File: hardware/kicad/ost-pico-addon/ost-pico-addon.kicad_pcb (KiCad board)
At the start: 2 copper layers, 70 x 60 mm, 13 parts, among them J1 Conn_01x09_Male, J2 104031-0811, J3 Conn_01x08_Male, J4 Conn_01x03_Male, U1 Pico

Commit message: pinout and routing changes
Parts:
- removed REF** (x6): MountingHole_2.2mm_M2_ISO7380_Pad, MountingHole:MountingHole_2.2mm_M2_ISO7380_Pad
- J3: value Conn_01x08_Male -> buttons; footprint Connector_PinHeader_2.54mm:PinHeader_1x08_P2.54mm_Vertical -> Connector_PinSocket_2.54mm:PinSocket_2x08_P2.54mm_Vertical
- moved J3 17.8 mm to (105.4, 129.5), turned to 0 degrees
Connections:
- J3 pad 1: +3.3V -> BUTTON_4
- J3 pad 3: ROT_1 -> BUTTON_3
- J3 pad 4: ROT_2 -> GND
- J3 pad 5: BUTTON_1 -> BUTTON_2
- J3 pad 6: BUTTON_2 -> GND
- J3 pad 7: BUTTON_3 -> BUTTON_1
- J3 pad 8: BUTTON_4 -> GND
- U1 pad 11: unconnected-(U1-Pad11) -> BUTTON_4
- U1 pad 12: unconnected-(U1-Pad12) -> BUTTON_3
- U1 pad 14: unconnected-(U1-Pad14) -> BUTTON_2
- U1 pad 15: unconnected-(U1-Pad15) -> BUTTON_1
- U1 pad 16: unconnected-(U1-Pad16) -> ROT_2
- U1 pad 17: unconnected-(U1-Pad17) -> ROT_1
- U1 pad 21: BUTTON_2 -> unconnected-(U1-GPIO16-Pad21)
- U1 pad 22: BUTTON_1 -> unconnected-(U1-GPIO17-Pad22)
- U1 pad 24: ROT_2 -> unconnected-(U1-GPIO18-Pad24)
- U1 pad 25: ROT_1 -> unconnected-(U1-GPIO19-Pad25)
- U1 pad 4: BUTTON_3 -> unconnected-(U1-GPIO2-Pad4)
- U1 pad 5: BUTTON_4 -> unconnected-(U1-GPIO3-Pad5)
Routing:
- net GND: track 223.4 -> 8.33 mm, vias 0 -> 2
- net SD_DET: track 139.9 -> 71.9 mm
- net BUTTON_2: track 82.8 -> 37.3 mm
- net BUTTON_1: track 79.0 -> 37.3 mm
- net ROT_1: track 78.4 -> 37.3 mm
- net ROT_2: track 68.4 -> 37.3 mm
- net BUTTON_4: track 57.7 -> 36.4 mm
- net BUTTON_3: track 50.7 -> 36.3 mm
- net +3.3V: track 133.4 -> 121.8 mm
- net SD_SPI_RX: track 36.6 -> 29.5 mm
- net SD_CS: track 33.6 -> 29.4 mm
- net SD_SPI_CLK: track 30.8 -> 29.3 mm
- added copper zone on B.Cu, net GND
- added copper zone on F.Cu, net GND

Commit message: change button port pinout
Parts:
- J3: footprint Connector_PinSocket_2.54mm:PinSocket_2x08_P2.54mm_Vertical -> Connector_PinHeader_2.54mm:PinHeader_2x07_P2.54mm_Vertical; moved to B.Cu
- turned J3 to 180 degrees
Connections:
- J3 pad 1: BUTTON_4 -> +3.3V
- J3 pad 11: ROT_1 -> ROT_2
- J3 pad 13: GND -> ROT_1
- J3 pad 14: GND -> ROT_BUTTON
- J3 pad 3: BUTTON_3 -> BUTTON_4
- J3 pad 5: BUTTON_2 -> BUTTON_3
- J3 pad 7: BUTTON_1 -> BUTTON_2
- J3 pad 9: ROT_2 -> BUTTON_1
- U1 pad 19: DBG_LED -> ROT_BUTTON
- U1 pad 20: SD_DET -> DBG_LED
- U1 pad 4: unconnected-(U1-GPIO2-Pad4) -> SD_DET
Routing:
- net ROT_BUTTON: track 0.00 -> 40.9 mm
- net SD_DET: track 71.9 -> 35.8 mm
- net +3.3V: track 121.8 -> 104.0 mm
- net GND: track 8.33 -> 3.28 mm, vias 2 -> 1
- net ROT_2: track 37.3 -> 36.3 mm
- net ROT_1: track 37.3 -> 36.3 mm
- net BUTTON_2: track 37.3 -> 36.3 mm
- net BUTTON_1: track 37.3 -> 36.3 mm
- net DBG_LED: track 12.9 -> 12.3 mm
- net BUTTON_4: track 36.4 -> 35.9 mm
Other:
- board text added: "3.3V BTN_4 BTN_3 BTN_2 BTN_1 ROT_2 ROT_1"
- board text added: "GND"
- board text added: "ROT_push"
- board text removed: "BTN_4 BTN_3 BTN_2 BTN_1 ROT_2 ROT_1 Gnd 3.3V"

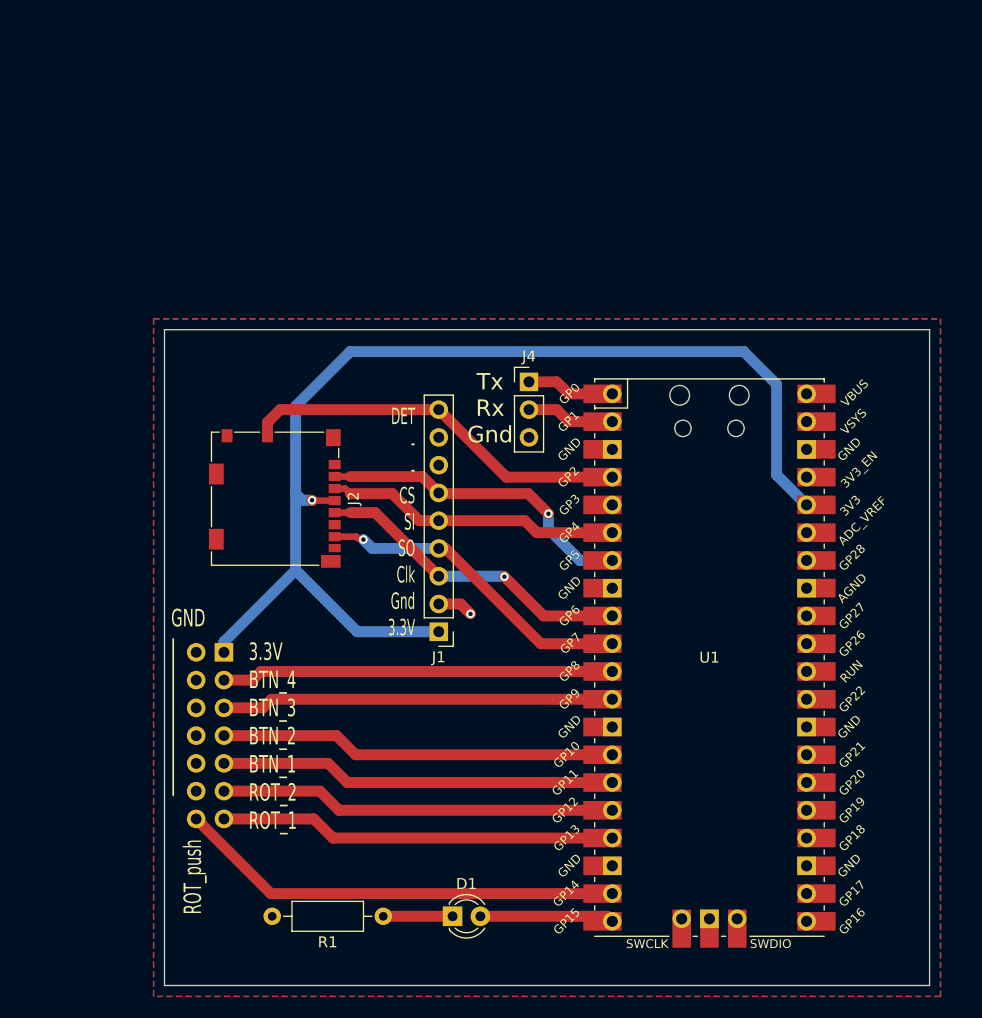
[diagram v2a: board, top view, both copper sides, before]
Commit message: editor v2 + usb host tests
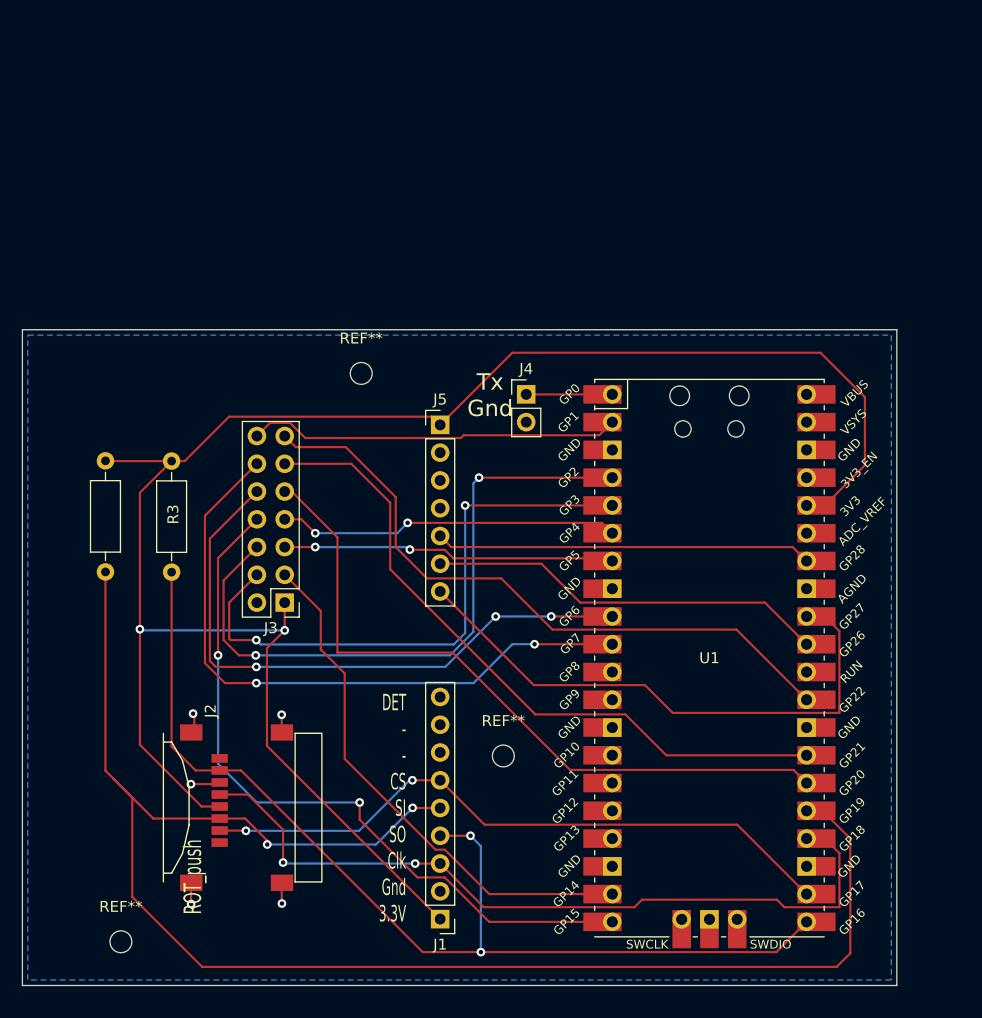
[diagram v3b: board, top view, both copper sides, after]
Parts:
- removed D1: LED, LED_THT:LED_D3.0mm
- removed R1: R_US, Resistor_THT:R_Axial_DIN0207_L6.3mm_D2.5mm_P10.16mm_Horizontal
- added J5: Conn_01x07_Pin, Connector_PinHeader_2.54mm:PinHeader_1x07_P2.54mm_Vertical, F.Cu at (125.2, 108.7)
- added R2: R_US, Resistor_THT:R_Axial_DIN0207_L6.3mm_D2.5mm_P10.16mm_Horizontal, F.Cu at (94.6, 112.0)
- added R3: R_US, Resistor_THT:R_Axial_DIN0207_L6.3mm_D2.5mm_P10.16mm_Horizontal, F.Cu at (100.7, 112.0)
- added REF**: MountingHole_2mm, MountingHole:MountingHole_2mm, F.Cu at (131.0, 139.0)
- added REF**: MountingHole_2mm, MountingHole:MountingHole_2mm, F.Cu at (96.0, 156.0)
- added REF**: MountingHole_2mm, MountingHole:MountingHole_2mm, F.Cu at (118.0, 104.0)
- J2: value 104031-0811 -> 47219-2001; footprint Connector_Card:microSD_HC_Molex_104031-0811 -> sdcard-libs:MOLEX_47219-2001
- J3: moved to F.Cu
- J4: value Conn_01x03_Male -> Conn_01x02_Pin; footprint Connector_PinHeader_2.54mm:PinHeader_1x03_P2.54mm_Vertical -> Connector_PinHeader_2.54mm:PinHeader_1x02_P2.54mm_Vertical
- moved J2 28.4 mm to (107.2, 143.7)
- moved J1 26.3 mm to (125.2, 153.9)
- moved J3 7.18 mm to (111.0, 125.0)
- moved J4 1.17 mm to (133.1, 105.9)
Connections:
- J1 pad 4: SD_SPI_RX -> SD_SPI_MISO
- J1 pad 5: SD_SPI_TX -> SD_SPI_MOSI
- J1 pad 9: SD_DET -> unconnected-(J1-Pin_9-Pad9)
- J2 pad 3: SD_SPI_TX -> SD_SPI_MOSI
- J2 pad 7: SD_SPI_RX -> SD_SPI_MISO
- J3 pad 10: GND -> ROT_1
- J3 pad 11: ROT_2 -> IO_2
- J3 pad 12: GND -> ROT_2
- J3 pad 13: ROT_1 -> IO_1
- J3 pad 3: BUTTON_4 -> IO_6
- J3 pad 4: GND -> KEY3
- J3 pad 5: BUTTON_3 -> IO_5
- J3 pad 6: GND -> KEY2
- J3 pad 7: BUTTON_2 -> IO_4
- J3 pad 8: GND -> KEY0
- J3 pad 9: BUTTON_1 -> IO_3
- J4 pad 2: DBG_RX -> GND
- U1 pad 10: SD_SPI_RX -> ROT_2
- U1 pad 11: BUTTON_4 -> unconnected-(U1-GPIO8-Pad11)
- U1 pad 12: BUTTON_3 -> unconnected-(U1-GPIO9-Pad12)
- U1 pad 14: BUTTON_2 -> unconnected-(U1-GPIO10-Pad14)
- U1 pad 15: BUTTON_1 -> unconnected-(U1-GPIO11-Pad15)
- U1 pad 16: ROT_2 -> unconnected-(U1-GPIO12-Pad16)
- U1 pad 17: ROT_1 -> unconnected-(U1-GPIO13-Pad17)
- U1 pad 19: ROT_BUTTON -> IO_6
- U1 pad 2: DBG_RX -> ROT_BUTTON
- U1 pad 20: DBG_LED -> KEY0
- U1 pad 21: unconnected-(U1-GPIO16-Pad21) -> SD_SPI_MISO
- U1 pad 22: unconnected-(U1-GPIO17-Pad22) -> SD_CS
- U1 pad 24: unconnected-(U1-GPIO18-Pad24) -> SD_SPI_CLK
- U1 pad 25: unconnected-(U1-GPIO19-Pad25) -> SD_SPI_MOSI
- U1 pad 26: unconnected-(U1-GPIO20-Pad26) -> IO_3
- U1 pad 27: unconnected-(U1-GPIO21-Pad27) -> IO_2
- U1 pad 29: unconnected-(U1-GPIO22-Pad29) -> IO_1
- U1 pad 31: unconnected-(U1-GPIO26_ADC0-Pad31) -> I2S_SCLK
- U1 pad 32: unconnected-(U1-GPIO27_ADC1-Pad32) -> I2S_LRCK
- U1 pad 34: unconnected-(U1-GPIO28_ADC2-Pad34) -> I2S_DATA
- U1 pad 4: SD_DET -> KEY2
- U1 pad 5: unconnected-(U1-GPIO3-Pad5) -> KEY3
- U1 pad 6: SD_SPI_TX -> IO_4
- U1 pad 7: SD_CS -> IO_5
- U1 pad 9: SD_SPI_CLK -> ROT_1
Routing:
- net SD_SPI_MOSI: track 0.00 -> 149.2 mm, vias 0 -> 2
- net SD_SPI_MISO: track 0.00 -> 96.8 mm, vias 0 -> 2
- net +3.3V: track 104.0 -> 175.3 mm, vias 1 -> 2
- net KEY0: track 0.00 -> 66.8 mm, vias 0 -> 2
- net IO_3: track 0.00 -> 65.0 mm
- net IO_2: track 0.00 -> 62.4 mm
- net KEY2: track 0.00 -> 60.6 mm, vias 0 -> 2
- net IO_1: track 0.00 -> 60.4 mm
- net KEY3: track 0.00 -> 54.3 mm, vias 0 -> 2
- net I2S_LRCK: track 0.00 -> 52.2 mm
- net IO_6: track 0.00 -> 48.7 mm
- net SD_SPI_CLK: track 29.3 -> 71.8 mm, vias 1 -> 2
- net I2S_SCLK: track 0.00 -> 36.6 mm
- net BUTTON_2: track 36.3 -> 0.00 mm
- net BUTTON_1: track 36.3 -> 0.00 mm
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- removed copper zone on F.Cu, net GND
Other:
- board size 70 x 60 mm -> 80 x 60 mm
- board text added: "Tx Gnd"
- board text removed: "3.3V BTN_4 BTN_3 BTN_2 BTN_1 ROT_2 ROT_1"
- board text removed: "GND"
- board text removed: "Tx Rx Gnd"

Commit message: Pico audio with 3 audio chips (complex)
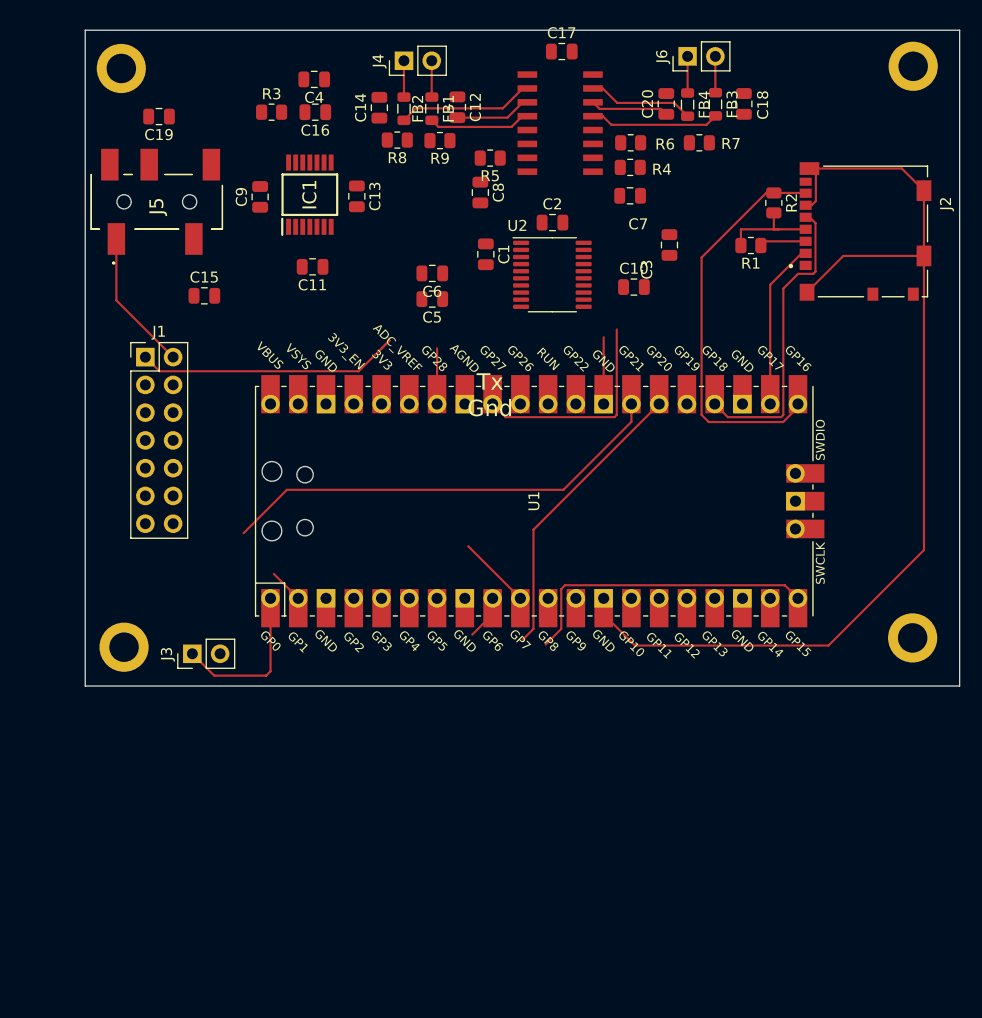
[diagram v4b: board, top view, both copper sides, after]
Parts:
- removed REF** (x3): MountingHole_2mm, MountingHole:MountingHole_2mm
- added C1: 2.2uF, Capacitor_SMD:C_0805_2012Metric, F.Cu at (129.4, 93.1)
- added C10: 1uF, Capacitor_SMD:C_0805_2012Metric, F.Cu at (142.9, 96.1)
- added C11: 1uF, Capacitor_SMD:C_0805_2012Metric, F.Cu at (113.5, 94.2)
- added C12: 270pF, Capacitor_SMD:C_0805_2012Metric, F.Cu at (126.8, 79.7)
- added C13: 47uF/6.3V/20%/X5R/C0805, Capacitor_SMD:C_0805_2012Metric, F.Cu at (117.6, 87.8)
- added C14: 270pF, Capacitor_SMD:C_0805_2012Metric, F.Cu at (119.7, 79.7)
- added C15: 47uF, Capacitor_SMD:C_0805_2012Metric, F.Cu at (103.7, 96.9)
- added C16: 47uF/6.3V/20%/X5R/C0805, Capacitor_SMD:C_0805_2012Metric, F.Cu at (113.8, 80.1)
- added C17: 100nF/50V/20%/Y5V/C0603, Capacitor_SMD:C_0805_2012Metric, F.Cu at (136.3, 74.5)
- added C18: 270pF, Capacitor_SMD:C_0805_2012Metric, F.Cu at (153.0, 79.3)
- added C19: 47uF, Capacitor_SMD:C_0805_2012Metric, F.Cu at (99.5, 80.5)
- added C2: 2.2uF, Capacitor_SMD:C_0805_2012Metric, F.Cu at (135.5, 90.2)
- added C20: 270pF, Capacitor_SMD:C_0805_2012Metric, F.Cu at (145.9, 79.3)
- added C3: 100nF, Capacitor_SMD:C_0805_2012Metric, F.Cu at (146.2, 92.2)
- added C4: 1uF, Capacitor_SMD:C_0805_2012Metric, F.Cu at (113.7, 77.1)
- added C5: 2.2uF, Capacitor_SMD:C_0805_2012Metric, F.Cu at (124.5, 97.2)
- added C6: 2.2uF, Capacitor_SMD:C_0805_2012Metric, F.Cu at (124.5, 94.8)
- added C7: 1uF, Capacitor_SMD:C_0805_2012Metric, F.Cu at (142.6, 87.8)
- added C8: 1uF, Capacitor_SMD:C_0805_2012Metric, F.Cu at (128.9, 87.5)
- added C9: 1uF, Capacitor_SMD:C_0805_2012Metric, F.Cu at (108.8, 87.8)
- added FB1: FB0805, Inductor_SMD:L_0805_2012Metric, F.Cu at (124.5, 79.8)
- added FB2: FB0805, Inductor_SMD:L_0805_2012Metric, F.Cu at (121.9, 79.8)
- added FB3: FB0805, Inductor_SMD:L_0805_2012Metric, F.Cu at (150.4, 79.4)
- added FB4: FB0805, Inductor_SMD:L_0805_2012Metric, F.Cu at (147.9, 79.4)
- added H1: MountingHole, MountingHole:MountingHole_2.7mm_M2.5_ISO14580_Pad, F.Cu at (96.0, 76.1)
- added H2: MountingHole, MountingHole:MountingHole_2.7mm_M2.5_ISO14580_Pad, F.Cu at (168.5, 75.9)
- added H3: MountingHole, MountingHole:MountingHole_2.7mm_M2.5_ISO14580_Pad, F.Cu at (168.4, 128.2)
- added H4: MountingHole, MountingHole:MountingHole_2.7mm_M2.5_ISO14580_Pad, F.Cu at (96.3, 129.1)
- added IC1: TPA6139A2PWR, audio:SOP65P640X120-14N, F.Cu at (113.3, 87.7)
- added J6: SPK_RIGHT, Connector_PinHeader_2.54mm:PinHeader_1x02_P2.54mm_Vertical, F.Cu at (147.9, 75.0)
- added R1: 10K, Resistor_SMD:R_0805_2012Metric, F.Cu at (153.7, 92.3)
- added R4: 10k, Resistor_SMD:R_0805_2012Metric, F.Cu at (142.6, 85.2)
- added R5: 10k, Resistor_SMD:R_0805_2012Metric, F.Cu at (129.8, 84.3)
- added R6: 1K, Resistor_SMD:R_0805_2012Metric, F.Cu at (142.7, 82.9)
- added R7: 1K(n.a.), Resistor_SMD:R_0805_2012Metric, F.Cu at (148.9, 82.9)
- added R8: 100K, Resistor_SMD:R_0805_2012Metric, F.Cu at (121.3, 82.7)
- added R9: 0K, Resistor_SMD:R_0805_2012Metric, F.Cu at (125.2, 82.7)
- added U2: PCM5102A, Package_SO:TSSOP-20_4.4x6.5mm_P0.65mm, F.Cu at (135.5, 95.0)
- added U3: PAM8003, audio:SO16, F.Cu at (136.2, 81.1)
- J1: value Conn_01x09_Male -> buttons; footprint Connector_PinHeader_2.54mm:PinHeader_1x09_P2.54mm_Vertical -> Connector_PinHeader_2.54mm:PinHeader_2x07_P2.54mm_Vertical
- J2: value 47219-2001 -> 104031-0811; footprint sdcard-libs:MOLEX_47219-2001 -> sdcard-libs:MOLEX_104031-0811
- J3: value buttons -> DBG_TX; footprint Connector_PinHeader_2.54mm:PinHeader_2x07_P2.54mm_Vertical -> Connector_PinHeader_2.54mm:PinHeader_1x02_P2.54mm_Vertical
- J4: value Conn_01x02_Pin -> SPK_LEFT
- J5: value Conn_01x07_Pin -> PJ-327U-SMT; footprint Connector_PinHeader_2.54mm:PinHeader_1x07_P2.54mm_Vertical -> audio:PJ327USMT
- R2: value R_US -> 10K; footprint Resistor_THT:R_Axial_DIN0207_L6.3mm_D2.5mm_P10.16mm_Horizontal -> Resistor_SMD:R_0805_2012Metric
- R3: value R_US -> 49K; footprint Resistor_THT:R_Axial_DIN0207_L6.3mm_D2.5mm_P10.16mm_Horizontal -> Resistor_SMD:R_0805_2012Metric
- moved J2 77.6 mm to (164.1, 91.0)
- moved R2 65.5 mm to (155.8, 88.4)
- moved J1 58.1 mm to (98.2, 102.5), turned to 0 degrees
- moved J5 37.9 mm to (93.3, 88.3), turned to 90 degrees
- moved R3 33.2 mm to (109.8, 80.1), turned to 0 degrees
- moved J4 32.5 mm to (121.9, 75.4), turned to 90 degrees
- moved U1 21.5 mm to (133.8, 115.7), turned to 90 degrees
- moved J3 9.66 mm to (102.5, 129.7), turned to 90 degrees
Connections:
- J1 pad 1: +3.3V -> +3V3
- J1 pad 3: SD_SPI_CLK -> IO_6
- J1 pad 4: SD_SPI_MISO -> KEY3
- J1 pad 5: SD_SPI_MOSI -> IO_5
- J1 pad 6: SD_CS -> KEY2
- J1 pad 7: unconnected-(J1-Pin_7-Pad7) -> IO_4
- J1 pad 8: unconnected-(J1-Pin_8-Pad8) -> KEY0
- J1 pad 9: unconnected-(J1-Pin_9-Pad9) -> IO_3
- J2 pad 4: +3.3V -> +3V3
- J3 pad 1: +3.3V -> DBG_TX
- J4 pad 1: DBG_TX -> Net-(J4-Pin_1)
- J4 pad 2: GND -> Net-(J4-Pin_2)
- J5 pad 3: unconnected-(J5-Pin_3-Pad3) -> Net-(C15-Pad1)
- J5 pad 5: I2S_DATA -> Net-(C19-Pad2)
- J5 pad 6: I2S_SCLK -> HP_DET
- R2 pad 1: +3.3V -> SD_SPI_MISO
- R2 pad 2: SD_SPI_MOSI -> +3V3
- R3 pad 1: +3.3V -> Net-(IC1-GAIN)
- R3 pad 2: SD_SPI_MISO -> GND
- U1 pad 36: +3.3V -> +3V3
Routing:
- net +3.3V: track 175.3 -> 0.00 mm, vias 2 -> 0
- net SD_SPI_MOSI: track 149.2 -> 4.26 mm, vias 2 -> 0
- net GND: track 10.3 -> 132.3 mm, vias 5 -> 0
- net KEY2: track 60.6 -> 0.00 mm, vias 2 -> 0
- net SD_SPI_MISO: track 96.8 -> 36.3 mm, vias 2 -> 0
- net IO_1: track 60.4 -> 0.00 mm
- net KEY3: track 54.3 -> 0.00 mm, vias 2 -> 0
- net ROT_2: track 59.7 -> 6.75 mm, vias 2 -> 0
- net ROT_1: track 56.2 -> 4.09 mm, vias 3 -> 0
- net IO_6: track 48.7 -> 0.00 mm
- net SD_CS: track 59.9 -> 15.3 mm, vias 2 -> 0
- net SD_SPI_CLK: track 71.8 -> 27.6 mm, vias 2 -> 0
- net KEY0: track 66.8 -> 28.0 mm, vias 2 -> 0
- net IO_3: track 65.0 -> 26.7 mm
- net I2S_SCLK: track 36.6 -> 0.30 mm
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- removed copper zone on B.Cu, net GND
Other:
- board text removed: "DET - - CS SI SO Clk Gnd 3.3V"
- board text removed: "ROT_push"
